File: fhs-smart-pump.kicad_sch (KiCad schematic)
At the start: 25 parts, among them J1 Screw_Terminal_01x09, J2 Conn_01x02, J3 Screw_Terminal_01x02, K1 G5NB, K2 G5NB, Q1 2SA1015, Q2 2SA1015, U1 LM2596T-5, U2 PC817, U3 ESP32-C3_SUPERMINI_TH, U4 PC817

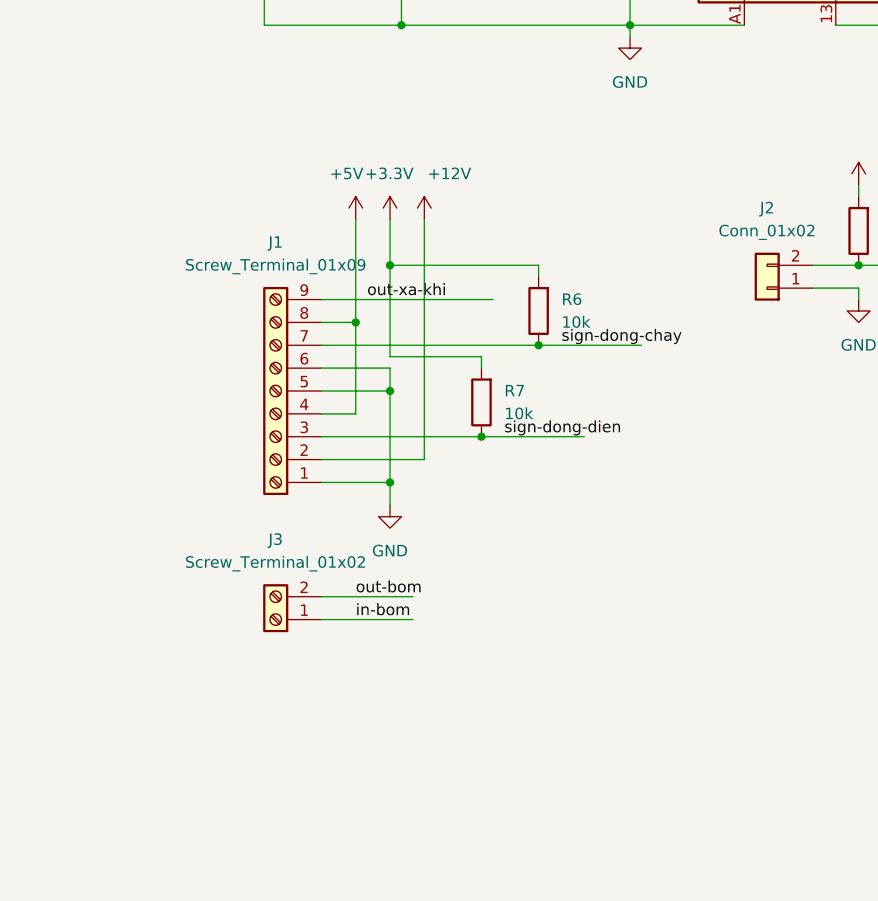
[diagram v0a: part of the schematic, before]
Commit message: đổi chân nguồn sang 5.5
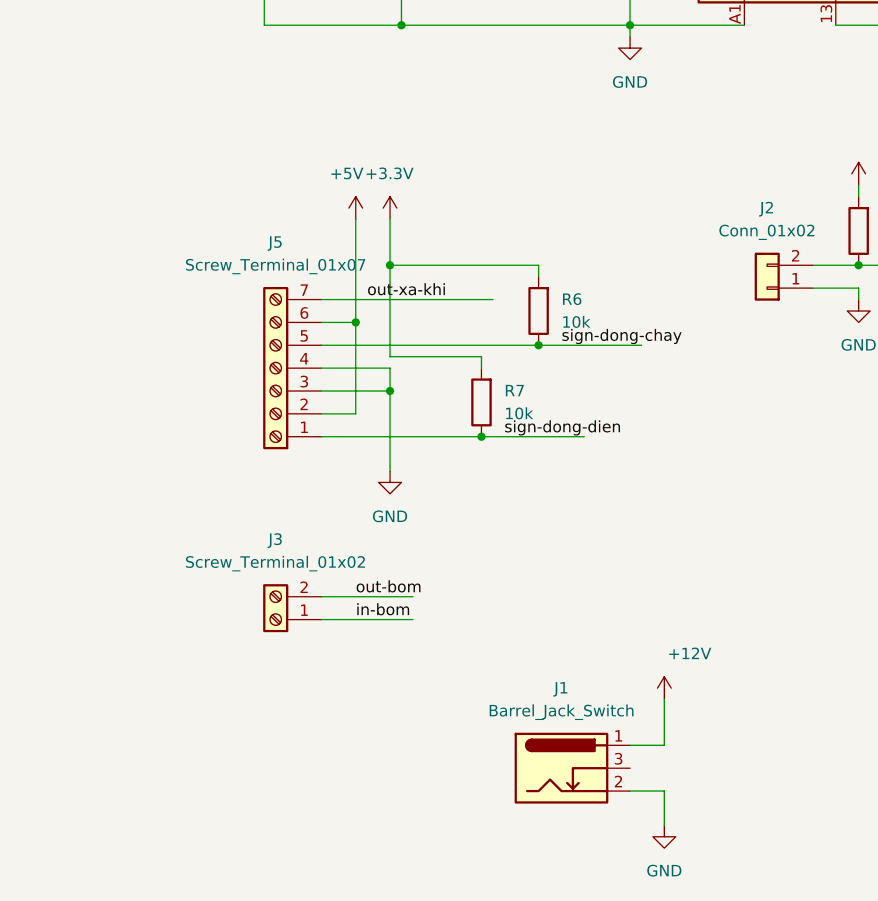
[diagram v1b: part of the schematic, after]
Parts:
- removed J1: Screw_Terminal_01x09, TerminalBlock:TerminalBlock_MaiXu_MX126-5.0-09P_1x09_P5.00mm, symbol Connector:Screw_Terminal_01x09
- added J1: Barrel_Jack_Switch, Connector_BarrelJack:BarrelJack_Horizontal, symbol Connector:Barrel_Jack_Switch
- added J5: Screw_Terminal_01x07, TerminalBlock:TerminalBlock_MaiXu_MX126-5.0-07P_1x07_P5.00mm, symbol Connector:Screw_Terminal_01x07
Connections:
- net +12V: now also J1.1
- net +5V: now also J5.2 (Pin_2), J5.6 (Pin_6)
- net GND: now also J1.2, J5.3 (Pin_3), J5.4 (Pin_4)
- net out-xa-khi: now also J5.7 (Pin_7)
- net sign-dong-chay: now also J5.5 (Pin_5)
- net sign-dong-dien: now also J5.1 (Pin_1)
